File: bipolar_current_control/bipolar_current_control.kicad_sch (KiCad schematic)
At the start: 31 parts, among them J1 Conn_01x10_Pin, J10 Output, J11 Conn_Coaxial, J2 Conn_01x10_Pin, J4 Conn_01x05, J6 Setpoint, J7 Monitor, J8 Current in +, J9 Current in -, Q1 TIP41C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

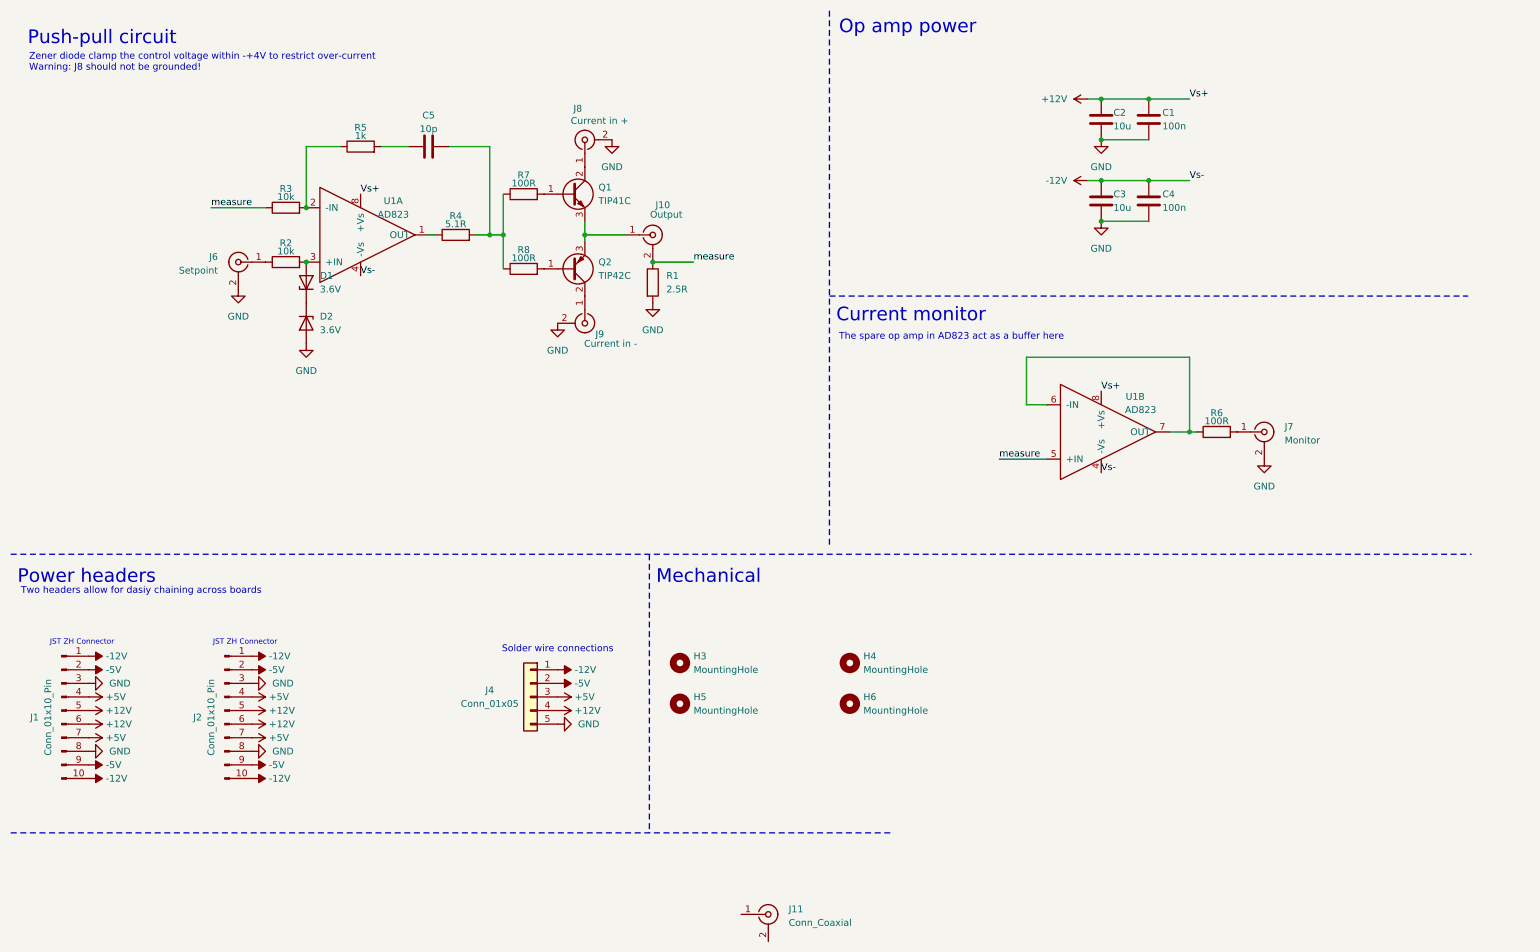
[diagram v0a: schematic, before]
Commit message: update circuit with op amp power selection
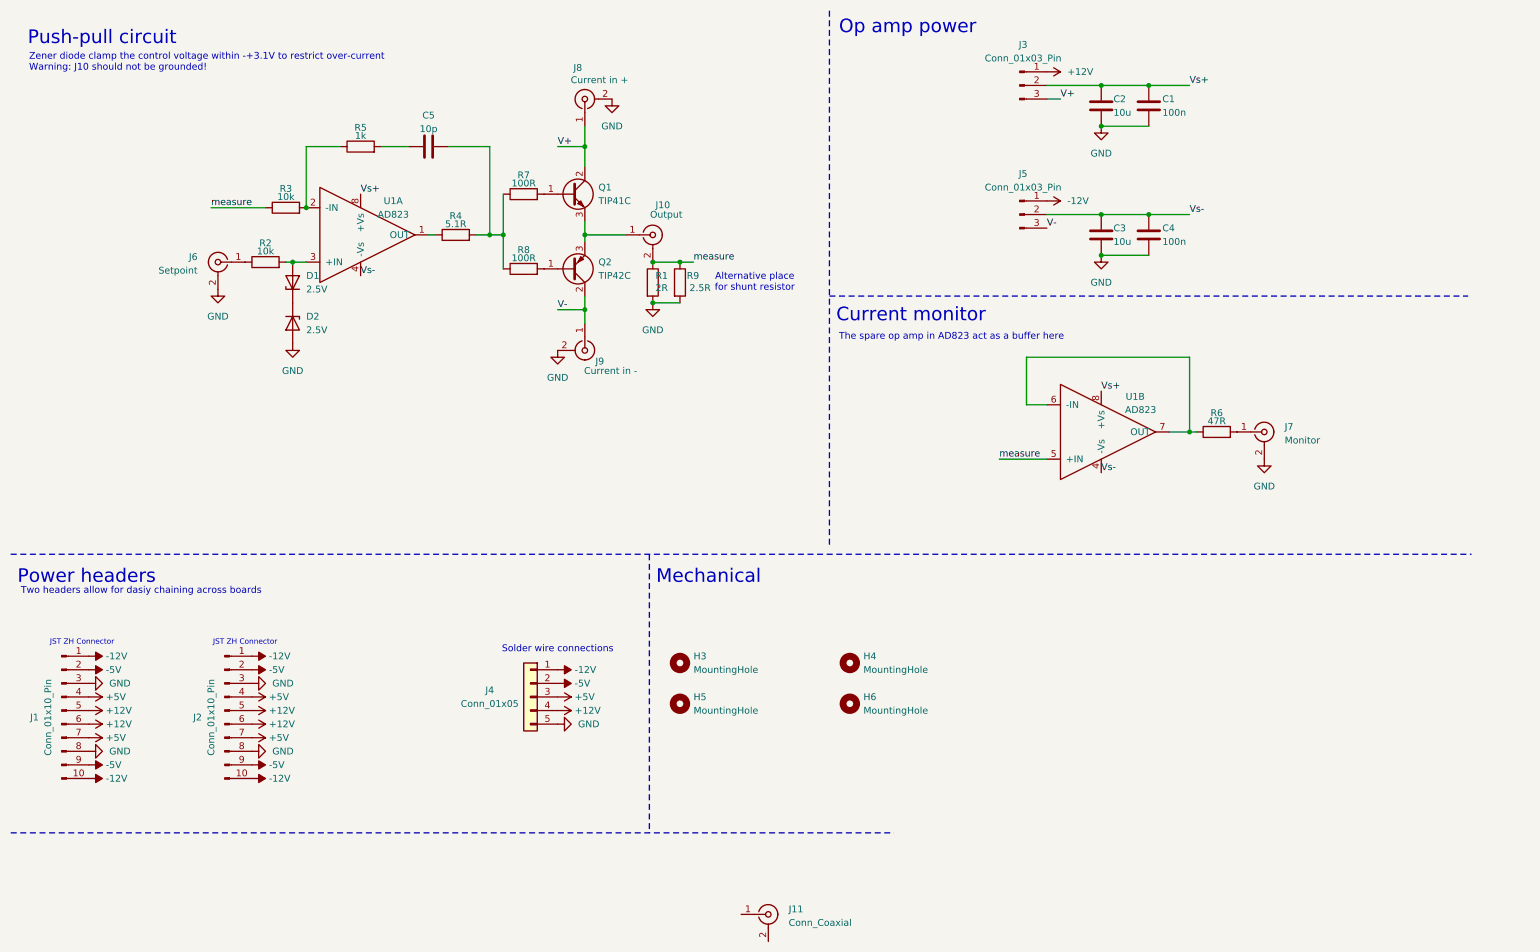
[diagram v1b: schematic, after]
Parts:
- added J3, J5: Conn_01x03_Pin, Connector_PinHeader_2.54mm:PinHeader_1x03_P2.54mm_Vertical, symbol Connector:Conn_01x03_Pin
- added R9: 2.5R, Resistor_THT:R_Axial_Power_L25.0mm_W9.0mm_P30.48mm, symbol Device:R
- D1, D2: value 3.6V -> 2.5V; LCSC (none) -> C118643
- R1: value 2.5R -> 2R; footprint Resistor_THT:R_Axial_Power_L25.0mm_W9.0mm_P30.48mm -> Package_TO_SOT_THT:TO-220F-2_Horizontal_TabUp; LCSC C22468858 -> C19708020
- R6: value 100R -> 47R; LCSC C57438 -> C119296
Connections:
- net +12V: now also J3.1 (Pin_1); no longer C1.1, C2.1, U1.8 (+Vs), U1.8 (+Vs)
- net -12V: now also J5.1 (Pin_1); no longer C3.1, C4.1, U1.4 (-Vs), U1.4 (-Vs)
- net GND: now also R9.2
- net measure: now also R9.1
- net V+: now reaches J8.1 (In), Q1.2 (C)
- net V+: now also J3.3 (Pin_3)
- net V-: now reaches J9.1 (In), Q2.2 (C)
- net V-: now also J5.3 (Pin_3)
- new net Vs+: C1.1, C2.1, J3.2 (Pin_2), U1.8 (+Vs), U1.8 (+Vs)
- new net Vs-: C3.1, C4.1, J5.2 (Pin_2), U1.4 (-Vs), U1.4 (-Vs)
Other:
- note added: "Alternative place for shunt resistor"
- note added: "Zener diode clamp the control voltage within -+3.1V to restrict over-current Warning: J10 should not be grounded!"
- note removed: "Zener diode clamp the control voltage within -+4V to restrict over-current Warning: J8 should not be grounded!"
- moved on the sheet: C1, C2, C3, C4, D1, D2, J6, J8, J9, R2

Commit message: add production files
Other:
- note added: "Alternative place for shunt resistor in other packages"
- note added: "Op amp power can be selected from +-12V and current power supply. Use current power supply when they are larger than +-12V to drive a large load. Make sure it does not exceed +-18V."
- note removed: "Alternative place for shunt resistor"
- moved on the sheet: C1, C2, J3
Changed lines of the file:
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@@
 		)
 	)
-	(text "Alternative place \nfor shunt resistor"
+	(text "Alternative place \nfor shunt resistor\nin other packages"
 		(exclude_from_sim no)
-		(at 151.13 63.5 0)
+		(at 152.908 63.754 0)
 		(effects
 			(font
@@
 		)
 	)
+	(text "Op amp power can be selected from +-12V and current power supply.\nUse current power supply when they are larger than +-12V to drive a large load.\nMake sure it does not exceed +-18V.\n"
+		(exclude_from_sim no)
+		(at 199.644 16.764 0)
+		(effects
+			(font
+				(size 1.27 1.27)
+			)
+			(justify left)
+		)
+	)
 	(text "JST ZH Connector"
 		(exclude_from_sim no)
@@
 	)
 	(junction
-		(at 224.79 26.67)
+		(at 224.79 31.75)
 		(diameter 0)
 		(color 0 0 0 0)
@@
 	)
 	(junction
-		(at 215.9 34.29)
+		(at 215.9 39.37)
 		(diameter 0)
 		(color 0 0 0 0)
@@
 	)
 	(junction
-		(at 215.9 26.67)
+		(at 215.9 31.75)
 		(diameter 0)
 		(color 0 0 0 0)
@@
 	(wire
 		(pts
-			(xy 215.9 34.29) (xy 224.79 34.29)
+			(xy 215.9 39.37) (xy 224.79 39.37)
 		)
 		(stroke
@@
 	(wire
 		(pts
-			(xy 232.41 26.67) (xy 224.79 26.67)
+			(xy 232.41 31.75) (xy 224.79 31.75)
 		)
 		(stroke
@@
 	(wire
 		(pts
-			(xy 224.79 26.67) (xy 215.9 26.67)
+			(xy 224.79 31.75) (xy 215.9 31.75)
 		)
 		(stroke
@@
 	(wire
 		(pts
-			(xy 208.28 29.21) (xy 205.74 29.21)
+			(xy 208.28 34.29) (xy 205.74 34.29)
 		)
 		(stroke
@@
 	(wire
 		(pts
-			(xy 205.74 26.67) (xy 215.9 26.67)
+			(xy 205.74 31.75) (xy 215.9 31.75)
 		)
 		(stroke
@@
 	)
 	(label "Vs+"
-		(at 232.41 26.67 0)
+		(at 232.41 31.75 0)
 		(effects
 			(font
@@
 	)
 	(label "V+"
-		(at 208.28 29.21 0)
+		(at 208.28 34.29 0)
 		(effects
 			(font
@@
 	(symbol
 		(lib_id "Connector:Conn_01x03_Pin")
-		(at 200.66 26.67 0)
+		(at 200.66 31.75 0)
 		(unit 1)
 		(exclude_from_sim no)
@@
 		(on_board yes)
 		(dnp no)
-		(fields_autoplaced yes)
 		(property "Reference" "J3"
-			(at 201.295 19.05 0)
+			(at 201.295 24.13 0)
 			(effects
 				(font
@@
 		)
 		(property "Value" "Conn_01x03_Pin"
-			(at 201.295 21.59 0)
+			(at 201.295 26.67 0)
 			(effects
 				(font
@@
 		)
 		(property "Footprint" "Connector_PinHeader_2.54mm:PinHeader_1x03_P2.54mm_Vertical"
-			(at 200.66 26.67 0)
+			(at 200.66 31.75 0)
 			(effects
 				(font
@@
 		)
 		(property "Datasheet" "~"
-			(at 200.66 26.67 0)
+			(at 200.66 31.75 0)
 			(effects
 				(font
@@
 		)
 		(property "Description" "Generic connector, single row, 01x03, script generated"
-			(at 200.66 26.67 0)
+			(at 200.66 31.75 0)
 			(effects
 				(font
@@
 	(symbol
 		(lib_id "Device:C")
-		(at 215.9 30.48 0)
+		(at 215.9 35.56 0)
 		(unit 1)
 		(exclude_from_sim no)
@@
 		(dnp no)
 		(property "Reference" "C2"
-			(at 218.186 29.21 0)
+			(at 218.186 34.29 0)
 			(effects
 				(font
@@
 		)
 		(property "Value" "10u"
-			(at 218.186 31.75 0)
+			(at 218.186 36.83 0)
 			(effects
 				(font
@@
 		)
 		(property "Footprint" "Capacitor_THT:C_Disc_D4.3mm_W1.9mm_P5.00mm"
-			(at 216.8652 34.29 0)
+			(at 216.8652 39.37 0)
 			(effects
 				(font
@@
 		)
 		(property "Datasheet" "~"
-			(at 215.9 30.48 0)
+			(at 215.9 35.56 0)
 			(effects
 				(font
@@
 		)
 		(property "Description" "Unpolarized capacitor"
-			(at 215.9 30.48 0)
+			(at 215.9 35.56 0)
 			(effects
 				(font
@@
 		)
 		(property "LCSC" ""
-			(at 215.9 30.48 0)
+			(at 215.9 35.56 0)
 			(effects
 				(font
@@
 	(symbol
 		(lib_id "power:+12V")
-		(at 205.74 24.13 270)
+		(at 205.74 29.21 270)
 		(unit 1)
 		(exclude_from_sim no)
@@
 		(fields_autoplaced yes)
 		(property "Reference" "#PWR029"
-			(at 201.93 24.13 0)
+			(at 201.93 29.21 0)
 			(effects
 				(font
@@
 		)
 		(property "Value" "+12V"
-			(at 209.55 24.1299 90)
+			(at 209.55 29.2099 90)
 			(effects
 				(font
@@
 		)
 		(property "Footprint" ""
-			(at 205.74 24.13 0)
+			(at 205.74 29.21 0)
 			(effects
 				(font
@@
 		)
 		(property "Datasheet" ""
-			(at 205.74 24.13 0)
+			(at 205.74 29.21 0)
 			(effects
 				(font
@@
 		)
 		(property "Description" "Power symbol creates a global label with name \"+12V\""
-			(at 205.74 24.13 0)
+			(at 205.74 29.21 0)
 			(effects
 				(font
@@
 	(symbol
 		(lib_id "power:GND")
-		(at 215.9 34.29 0)
+		(at 215.9 39.37 0)
 		(unit 1)
 		(exclude_from_sim no)
@@
 		(fields_autoplaced yes)
 		(property "Reference" "#PWR030"
-			(at 215.9 40.64 0)
+			(at 215.9 45.72 0)
 			(effects
 				(font
@@
 		)
 		(property "Value" "GND"
-			(at 215.9 39.37 0)
+			(at 215.9 44.45 0)
 			(effects
 				(font
@@
 		)
 		(property "Footprint" ""
-			(at 215.9 34.29 0)
+			(at 215.9 39.37 0)
 			(effects
 				(font
@@
 		)
 		(property "Datasheet" ""
-			(at 215.9 34.29 0)
+			(at 215.9 39.37 0)
 			(effects
 				(font
@@
 		)
 		(property "Description" "Power symbol creates a global label with name \"GND\" , ground"
-			(at 215.9 34.29 0)
+			(at 215.9 39.37 0)
 			(effects
 				(font
@@
 	(symbol
 		(lib_id "Device:C")
-		(at 224.79 30.48 0)
+		(at 224.79 35.56 0)
 		(unit 1)
 		(exclude_from_sim no)
@@
 		(dnp no)
 		(property "Reference" "C1"
-			(at 227.33 29.21 0)
+			(at 227.33 34.29 0)
 			(effects
 				(font
@@
 		)
 		(property "Value" "100n"
-			(at 227.33 31.75 0)
+			(at 227.33 36.83 0)
 			(effects
 				(font
@@
 		)
 		(property "Footprint" "Capacitor_THT:C_Disc_D4.3mm_W1.9mm_P5.00mm"
-			(at 225.7552 34.29 0)
+			(at 225.7552 39.37 0)
 			(effects
 				(font
@@
 		)
 		(property "Datasheet" "~"
-			(at 224.79 30.48 0)
+			(at 224.79 35.56 0)
 			(effects
 				(font
@@
 		)
 		(property "Description" "Unpolarized capacitor"
-			(at 224.79 30.48 0)
+			(at 224.79 35.56 0)
 			(effects
 				(font
@@
 		)
 		(property "LCSC" ""
-			(at 224.79 30.48 0)
+			(at 224.79 35.56 0)
 			(effects
 				(font

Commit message: add design with ADA4700-1
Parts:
- C1, C4: LCSC (none) -> C84772
- C2, C3: LCSC (none) -> C2761740
- J3, J5: LCSC (none) -> C5360899
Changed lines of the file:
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@@
 			)
 		)
+		(property "LCSC" "C5360899 "
+			(at 200.66 31.75 0)
+			(effects
+				(font
+					(size 1.27 1.27)
+				)
+				(hide yes)
+			)
+		)
 		(pin "1"
 		)
@@
 			)
 		)
-		(property "LCSC" ""
+		(property "LCSC" "C2761740 "
 			(at 215.9 35.56 0)
 			(effects
@@
 			)
 		)
-		(property "LCSC" ""
+		(property "LCSC" "C84772"
 			(at 224.79 54.61 0)
 			(effects
@@
 			)
 		)
-		(property "LCSC" ""
+		(property "LCSC" "C2761740 "
 			(at 215.9 54.61 0)
 			(effects
@@
 			)
 		)
+		(property "LCSC" "C5360899 "
+			(at 200.66 50.8 0)
+			(effects
+				(font
+					(size 1.27 1.27)
+				)
+				(hide yes)
+			)
+		)
 		(pin "1"
 		)
@@
 			)
 		)
-		(property "LCSC" ""
+		(property "LCSC" "C84772"
 			(at 224.79 35.56 0)
 			(effects
